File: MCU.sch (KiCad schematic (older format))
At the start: 32 parts, among them IC1 STM32G474RET6, SW1 RST, SW2 SW_DIP_x04, U14 MCP2562-E-SN, U15 ST1480ABDR, U16 AM26LV32ACPWR, U17 SI8621AB-B-ISR, Y1 Resonator_Small

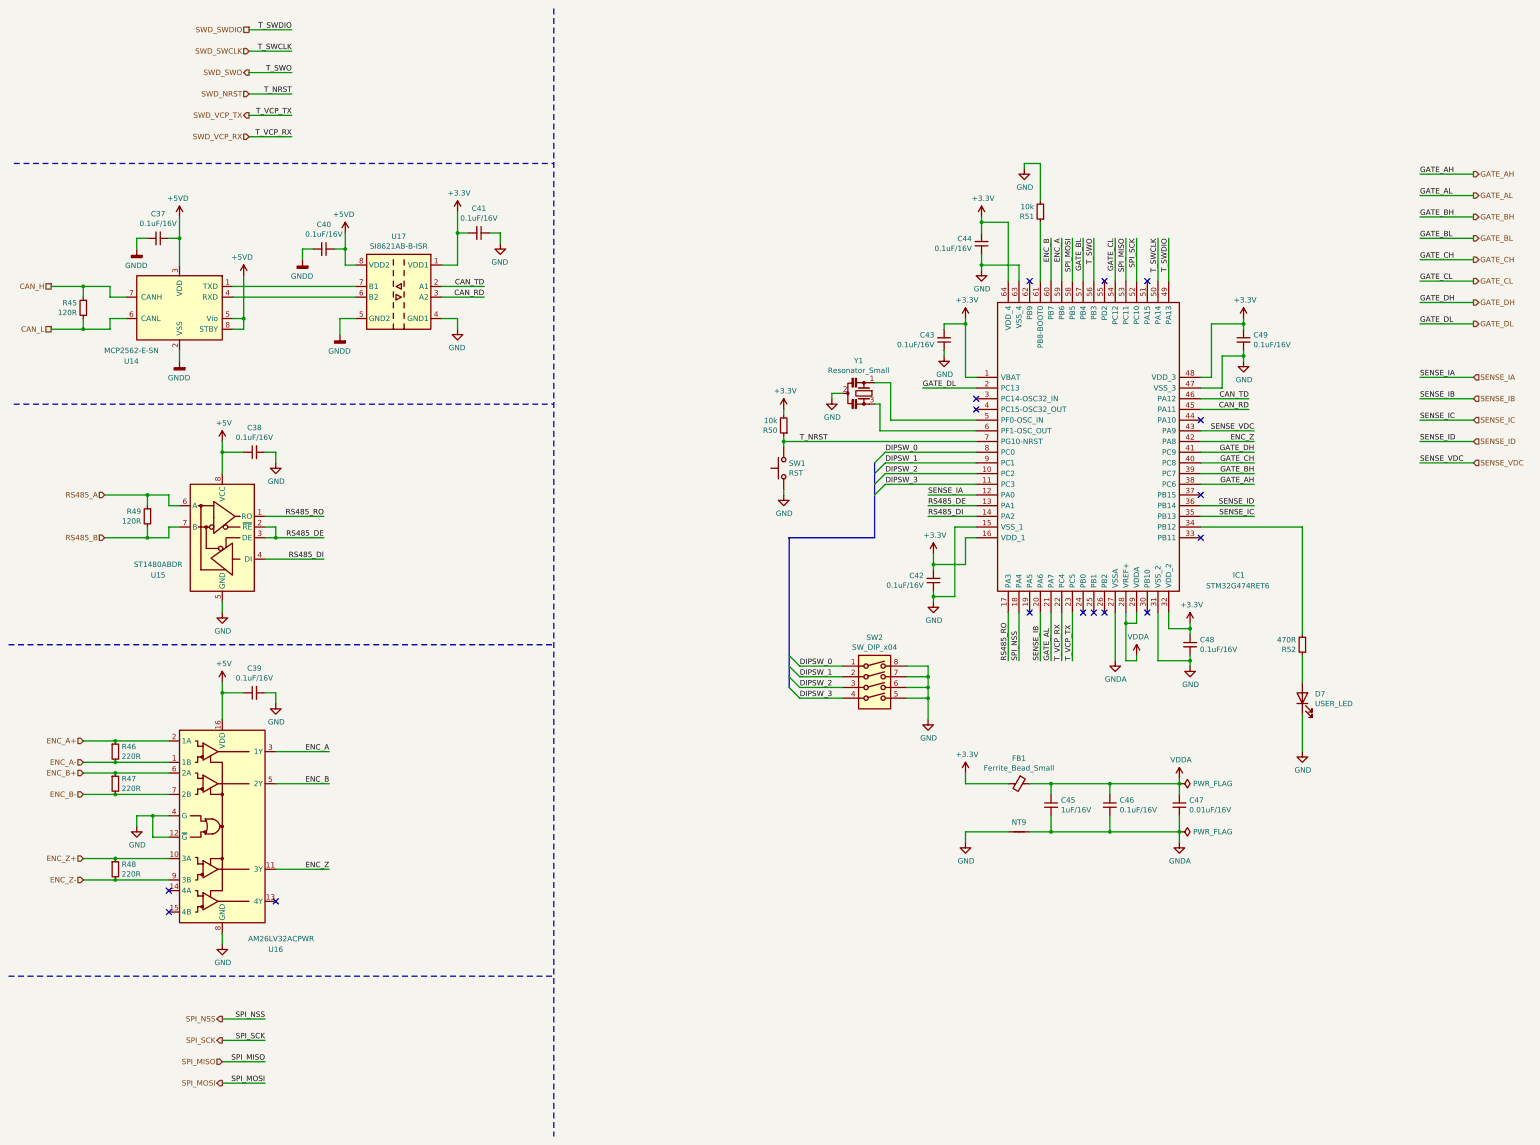
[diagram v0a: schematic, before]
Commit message: Update: 回路図、DCリンクCap1つ削除、アノテーションリセット
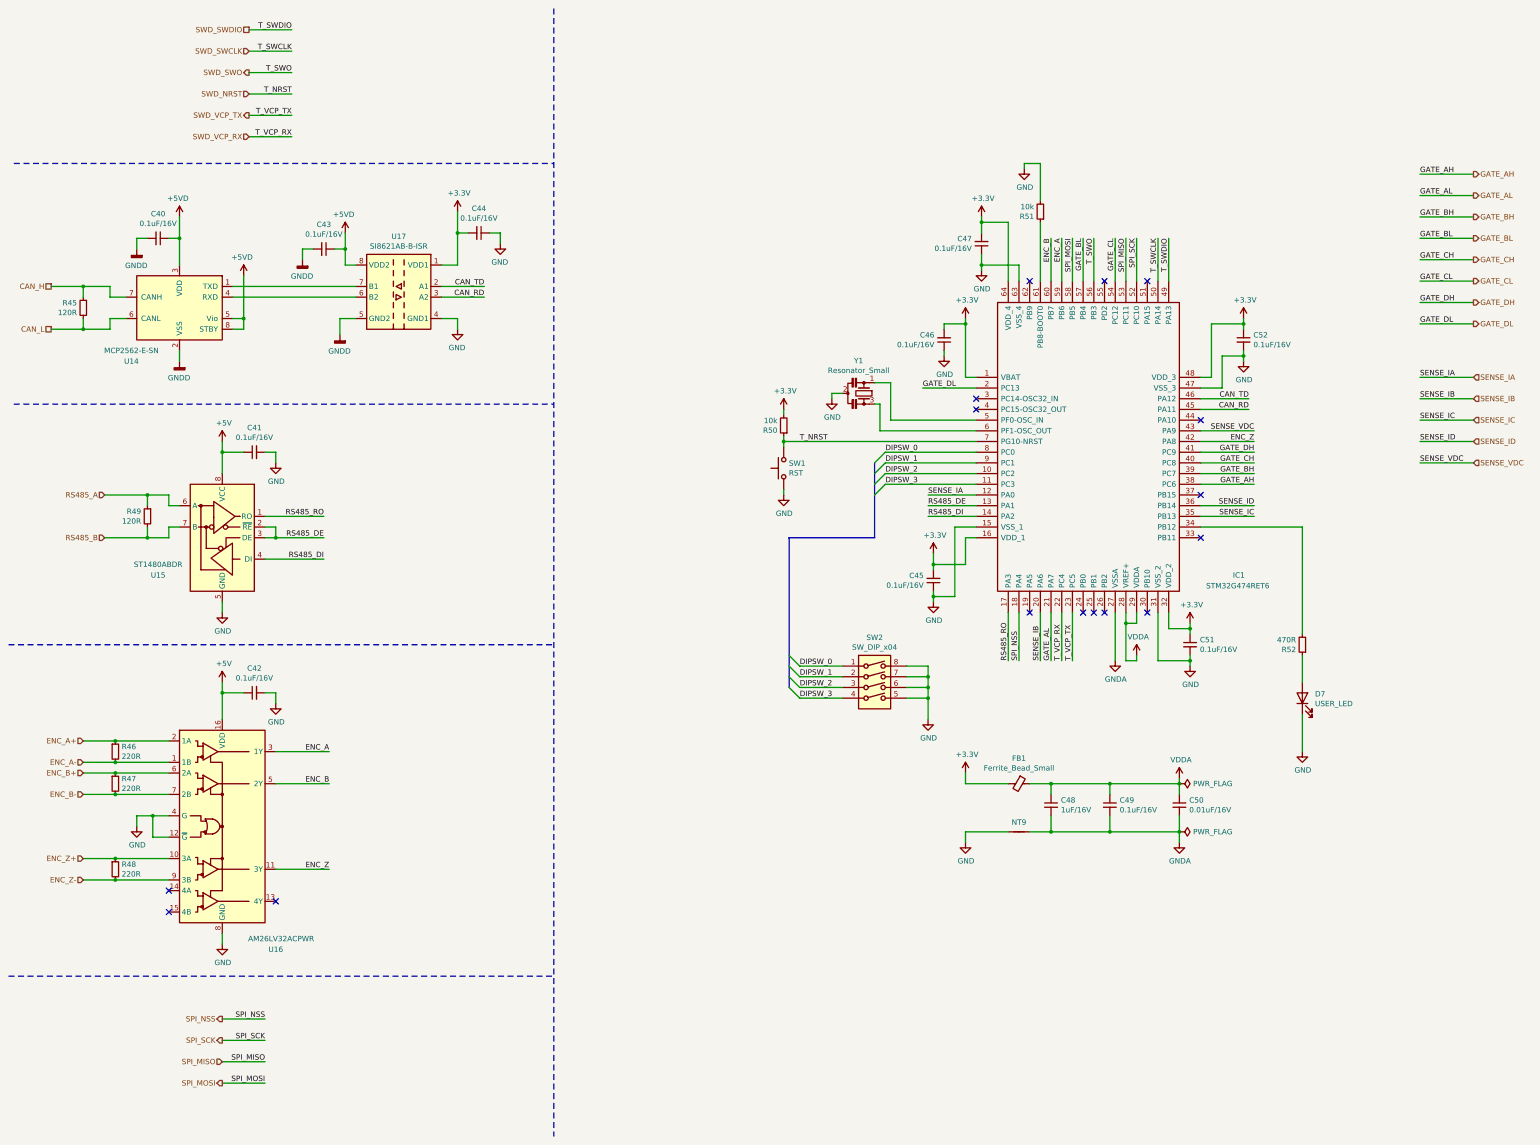
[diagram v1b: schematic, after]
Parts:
- renumbered C37 to C40, C38 to C41, C39 to C42, C40 to C43, C41 to C44, C42 to C45, C43 to C46, C44 to C47, C45 to C48, C46 to C49, C47 to C50, C48 to C51, C49 to C52
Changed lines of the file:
@@
 P 9750 3000
 AR Path="/6081BB0D" Ref="#PWR?"  Part="1"
-AR Path="/607D8C01/6081BB0D" Ref="#PWR0100"  Part="1"
-F 0 "#PWR0100" H 9750 2750 50  0001 C CNN
+AR Path="/607D8C01/6081BB0D" Ref="#PWR0102"  Part="1"
+F 0 "#PWR0102" H 9750 2750 50  0001 C CNN
 F 1 "GND" H 9755 2827 50  0000 C CNN
 F 2 "" H 9750 3000 50  0001 C CNN
@@
 P 9600 8350
 AR Path="/6081BB3C" Ref="#PWR?"  Part="1"
-AR Path="/607D8C01/6081BB3C" Ref="#PWR0102"  Part="1"
-F 0 "#PWR0102" H 9600 8100 50  0001 C CNN
+AR Path="/607D8C01/6081BB3C" Ref="#PWR0100"  Part="1"
+F 0 "#PWR0100" H 9600 8100 50  0001 C CNN
 F 1 "GND" H 9605 8177 50  0000 C CNN
 F 2 "" H 9600 8350 50  0001 C CNN
@@
 P 10400 8000
 AR Path="/6081BB44" Ref="C?"  Part="1"
-AR Path="/607D8C01/6081BB44" Ref="C45"  Part="1"
-F 0 "C45" H 10492 8046 50  0000 L CNN
+AR Path="/607D8C01/6081BB44" Ref="C48"  Part="1"
+F 0 "C48" H 10492 8046 50  0000 L CNN
 F 1 "1uF/16V" H 10492 7955 50  0000 L CNN
 F 2 "Capacitor_SMD:C_0603_1608Metric" H 10400 8000 50  0001 C CNN
@@
 P 10950 8000
 AR Path="/6081BB4A" Ref="C?"  Part="1"
-AR Path="/607D8C01/6081BB4A" Ref="C46"  Part="1"
-F 0 "C46" H 11042 8046 50  0000 L CNN
+AR Path="/607D8C01/6081BB4A" Ref="C49"  Part="1"
+F 0 "C49" H 11042 8046 50  0000 L CNN
 F 1 "0.1uF/16V" H 11042 7955 50  0000 L CNN
 F 2 "Capacitor_SMD:C_0603_1608Metric" H 10950 8000 50  0001 C CNN
@@
 P 11600 8000
 AR Path="/6081BB50" Ref="C?"  Part="1"
-AR Path="/607D8C01/6081BB50" Ref="C47"  Part="1"
-F 0 "C47" H 11692 8046 50  0000 L CNN
+AR Path="/607D8C01/6081BB50" Ref="C50"  Part="1"
+F 0 "C50" H 11692 8046 50  0000 L CNN
 F 1 "0.01uF/16V" H 11692 7955 50  0000 L CNN
 F 2 "Capacitor_SMD:C_0603_1608Metric" H 11600 8000 50  0001 C CNN
@@
 P 9400 3650
 AR Path="/6081BB7F" Ref="C?"  Part="1"
-AR Path="/607D8C01/6081BB7F" Ref="C43"  Part="1"
-F 0 "C43" H 9309 3604 50  0000 R CNN
+AR Path="/607D8C01/6081BB7F" Ref="C46"  Part="1"
+F 0 "C46" H 9309 3604 50  0000 R CNN
 F 1 "0.1uF/16V" H 9309 3695 50  0000 R CNN
 F 2 "Capacitor_SMD:C_0603_1608Metric" H 9400 3650 50  0001 C CNN
@@
 P 9300 5900
 AR Path="/6081BB8A" Ref="C?"  Part="1"
-AR Path="/607D8C01/6081BB8A" Ref="C42"  Part="1"
-F 0 "C42" H 9209 5854 50  0000 R CNN
+AR Path="/607D8C01/6081BB8A" Ref="C45"  Part="1"
+F 0 "C45" H 9209 5854 50  0000 R CNN
 F 1 "0.1uF/16V" H 9209 5945 50  0000 R CNN
 F 2 "Capacitor_SMD:C_0603_1608Metric" H 9300 5900 50  0001 C CNN
@@
 P 11700 6500
 AR Path="/6081BB95" Ref="C?"  Part="1"
-AR Path="/607D8C01/6081BB95" Ref="C48"  Part="1"
-F 0 "C48" H 11792 6546 50  0000 L CNN
+AR Path="/607D8C01/6081BB95" Ref="C51"  Part="1"
+F 0 "C51" H 11792 6546 50  0000 L CNN
 F 1 "0.1uF/16V" H 11792 6455 50  0000 L CNN
 F 2 "Capacitor_SMD:C_0603_1608Metric" H 11700 6500 50  0001 C CNN
@@
 P 12200 3650
 AR Path="/6081BBB0" Ref="C?"  Part="1"
-AR Path="/607D8C01/6081BBB0" Ref="C49"  Part="1"
-F 0 "C49" H 12292 3696 50  0000 L CNN
+AR Path="/607D8C01/6081BBB0" Ref="C52"  Part="1"
+F 0 "C52" H 12292 3696 50  0000 L CNN
 F 1 "0.1uF/16V" H 12292 3605 50  0000 L CNN
 F 2 "Capacitor_SMD:C_0603_1608Metric" H 12200 3650 50  0001 C CNN
@@
 P 9750 2750
 AR Path="/6081BC36" Ref="C?"  Part="1"
-AR Path="/607D8C01/6081BC36" Ref="C44"  Part="1"
-F 0 "C44" H 9659 2704 50  0000 R CNN
+AR Path="/607D8C01/6081BC36" Ref="C47"  Part="1"
+F 0 "C47" H 9659 2704 50  0000 R CNN
 F 1 "0.1uF/16V" H 9659 2795 50  0000 R CNN
 F 2 "Capacitor_SMD:C_0603_1608Metric" H 9750 2750 50  0001 C CNN
@@
 	4850 2950 4700 2950
 $Comp
-L Device:C_Small C37
+L Device:C_Small C40
 U 1 1 5D63A863
 P 2050 2700
-F 0 "C37" V 2279 2700 50  0000 C CNN
+F 0 "C40" V 2279 2700 50  0000 C CNN
 F 1 "0.1uF/16V" V 2188 2700 50  0000 C CNN
 F 2 "Capacitor_SMD:C_0603_1608Metric" H 2050 2700 50  0001 C CNN
@@
 	3800 2950 3900 2950
 $Comp
-L Device:C_Small C40
+L Device:C_Small C43
 U 1 1 5D654E8E
 P 3600 2800
-F 0 "C40" V 3829 2800 50  0000 C CNN
+F 0 "C43" V 3829 2800 50  0000 C CNN
 F 1 "0.1uF/16V" V 3738 2800 50  0000 C CNN
 F 2 "Capacitor_SMD:C_0603_1608Metric" H 3600 2800 50  0001 C CNN
@@
 	3400 2800 3400 2900
 $Comp
-L Device:C_Small C41
+L Device:C_Small C44
 U 1 1 5D66021A
 P 5050 2650
-F 0 "C41" V 5279 2650 50  0000 C CNN
+F 0 "C44" V 5279 2650 50  0000 C CNN
 F 1 "0.1uF/16V" V 5188 2650 50  0000 C CNN
 F 2 "Capacitor_SMD:C_0603_1608Metric" H 5050 2650 50  0001 C CNN
@@
 RS485_DI
 $Comp
-L Device:C_Small C38
+L Device:C_Small C41
 U 1 1 6207F667
 P 2950 4700
-F 0 "C38" V 3179 4700 50  0000 C CNN
+F 0 "C41" V 3179 4700 50  0000 C CNN
 F 1 "0.1uF/16V" V 3088 4700 50  0000 C CNN
 F 2 "Capacitor_SMD:C_0603_1608Metric" H 2950 4700 50  0001 C CNN
@@
 	2650 6850 2650 6950
 $Comp
-L Device:C_Small C39
+L Device:C_Small C42
 U 1 1 62180D5B
 P 2950 6950
-F 0 "C39" V 3179 6950 50  0000 C CNN
+F 0 "C42" V 3179 6950 50  0000 C CNN
 F 1 "0.1uF/16V" V 3088 6950 50  0000 C CNN
 F 2 "Capacitor_SMD:C_0603_1608Metric" H 2950 6950 50  0001 C CNN
@@
 P 9600 7700
 AR Path="/63184AE5" Ref="#PWR?"  Part="1"
-AR Path="/607D8C01/63184AE5" Ref="#PWR0101"  Part="1"
-F 0 "#PWR0101" H 9600 7550 50  0001 C CNN
+AR Path="/607D8C01/63184AE5" Ref="#PWR099"  Part="1"
+F 0 "#PWR099" H 9600 7550 50  0001 C CNN
 F 1 "+3.3V" H 9615 7873 50  0000 C CNN
 F 2 "" H 9600 7700 50  0001 C CNN
@@
 P 9750 2500
 AR Path="/6321E3A4" Ref="#PWR?"  Part="1"
-AR Path="/607D8C01/6321E3A4" Ref="#PWR099"  Part="1"
-F 0 "#PWR099" H 9750 2350 50  0001 C CNN
+AR Path="/607D8C01/6321E3A4" Ref="#PWR0101"  Part="1"
+F 0 "#PWR0101" H 9750 2350 50  0001 C CNN
 F 1 "+3.3V" H 9765 2673 50  0000 C CNN
 F 2 "" H 9750 2500 50  0001 C CNN
@@
 NoConn ~ 10200 3100
 $Comp
-L power:PWR_FLAG #FLG0109
+L power:PWR_FLAG #FLG08
 U 1 1 63940CAC
 P 11600 8250
-F 0 "#FLG0109" H 11600 8325 50  0001 C CNN
+F 0 "#FLG08" H 11600 8325 50  0001 C CNN
 F 1 "PWR_FLAG" V 11600 8378 50  0000 L CNN
 F 2 "" H 11600 8250 50  0001 C CNN
@@
 $EndComp
 $Comp
-L power:PWR_FLAG #FLG0110
+L power:PWR_FLAG #FLG07
 U 1 1 63941F34
 P 11600 7800
-F 0 "#FLG0110" H 11600 7875 50  0001 C CNN
+F 0 "#FLG07" H 11600 7875 50  0001 C CNN
 F 1 "PWR_FLAG" V 11600 7928 50  0000 L CNN
 F 2 "" H 11600 7800 50  0001 C CNN

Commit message: Update: アナログリファレンスをLDOからに変更
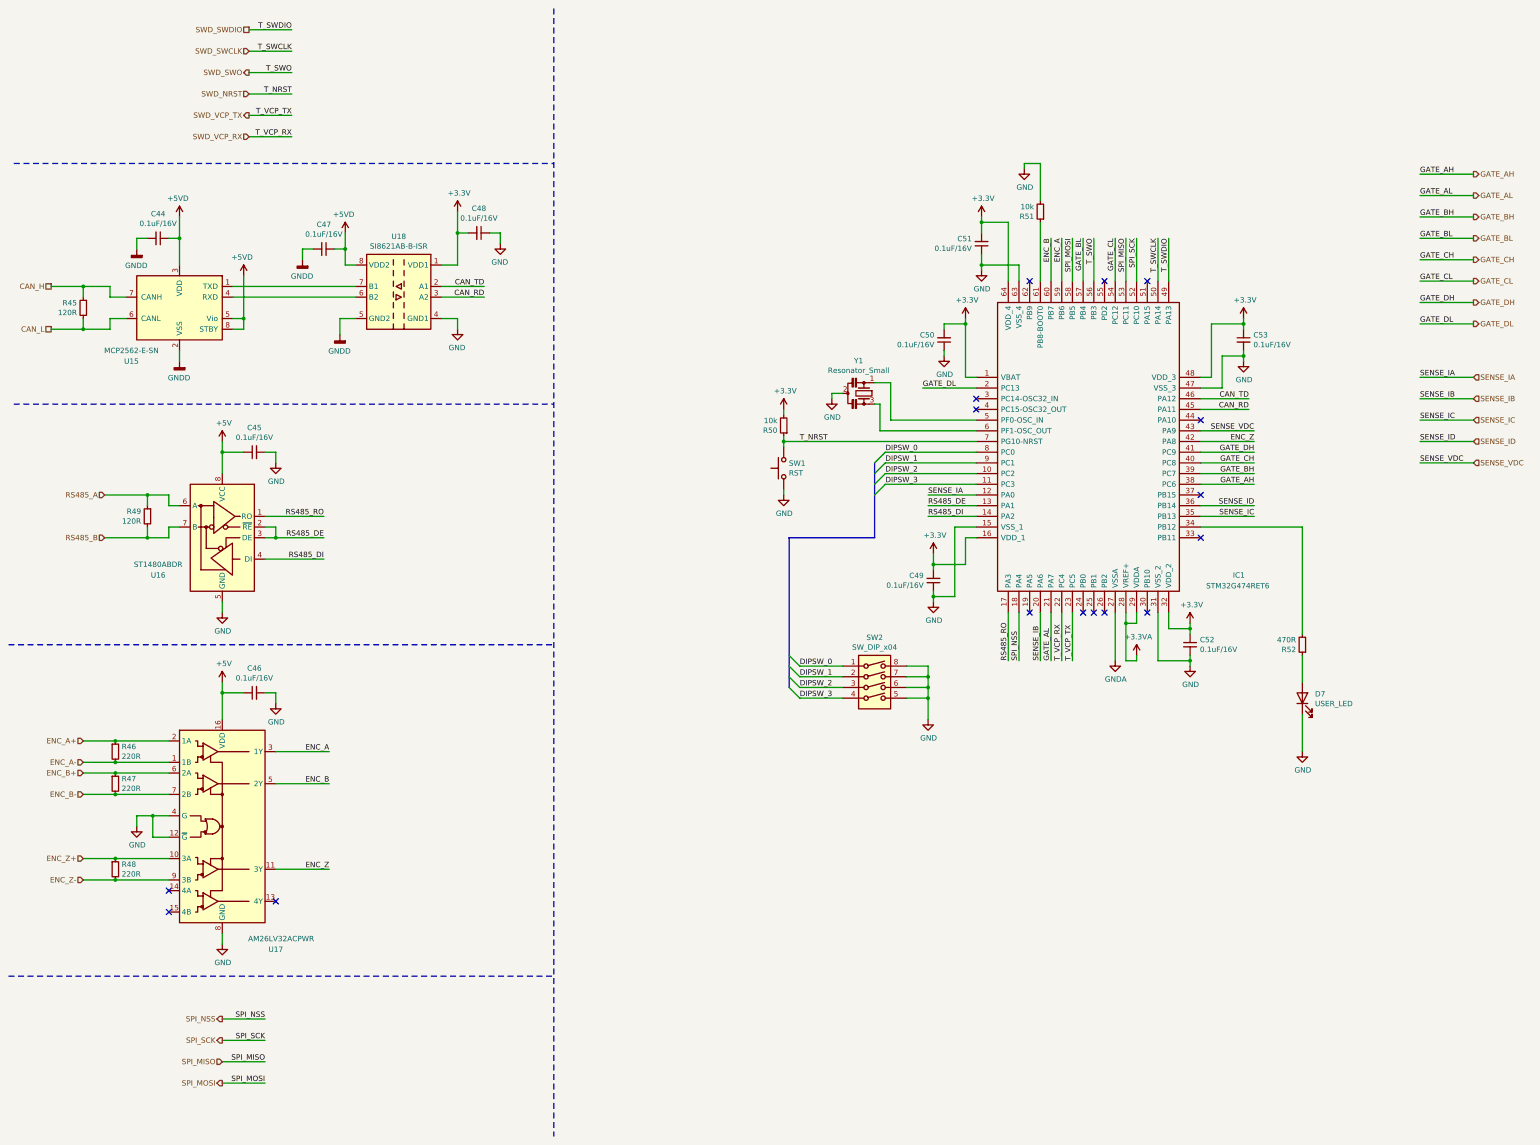
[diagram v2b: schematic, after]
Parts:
- removed C48: 1uF/16V, Capacitor_SMD:C_0603_1608Metric, symbol Device:C_Small
- removed C49: 0.1uF/16V, Capacitor_SMD:C_0603_1608Metric, symbol Device:C_Small
- removed C50: 0.01uF/16V, Capacitor_SMD:C_0603_1608Metric, symbol Device:C_Small
- removed FB1: Ferrite_Bead_Small, Inductor_SMD:L_0603_1608Metric, symbol Device:Ferrite_Bead_Small
- removed NT9: Net-Tie_2, NetTie:NetTie-2_SMD_Pad0.5mm, symbol Device:Net-Tie_2
- renumbered C40 to C44, C41 to C45, C42 to C46, C43 to C47, C44 to C48, C45 to C49, C46 to C50, C47 to C51, C51 to C52, C52 to C53, U14 to U15, U15 to U16, U16 to U17, U17 to U18
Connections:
- net VDDA renamed +3.3VA

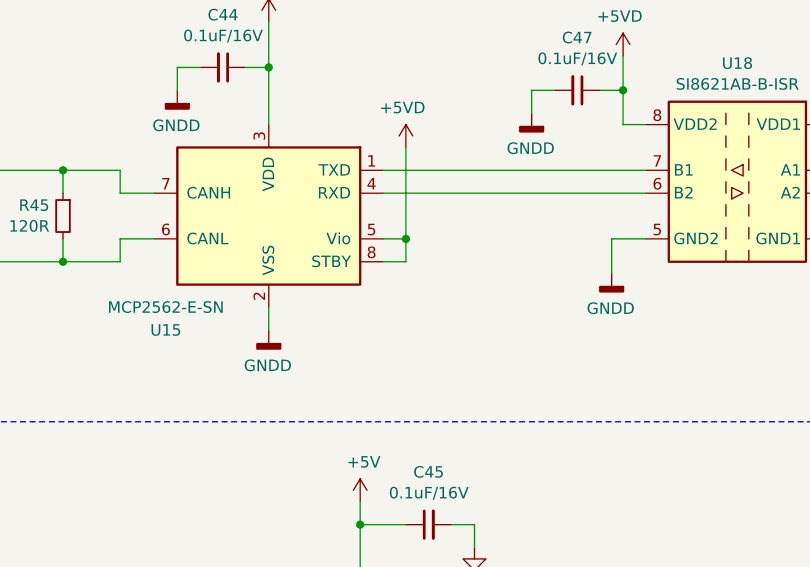
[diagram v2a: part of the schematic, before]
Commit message: wip CAN STBYピン修正
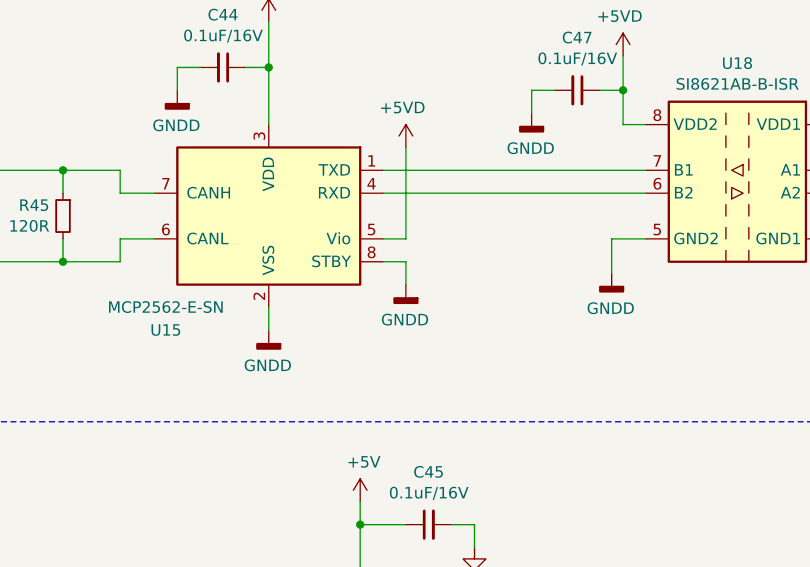
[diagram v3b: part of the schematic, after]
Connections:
- net +5VD: no longer U15.8 (STBY)
- net GNDD: now also U15.8 (STBY)
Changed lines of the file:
@@
 	2750 3550 2850 3550
 Wire Wire Line
-	2850 3550 2850 3450
-Connection ~ 2850 3450
+	2850 3650 2850 3550
 Wire Wire Line
 	3900 3150 2750 3150
@@
 	1    0    0    -1
 $EndComp
+$Comp
+L power:GNDD #PWR?
+U 1 1 60CCC792
+P 2850 3650
+AR Path="/60CCC792" Ref="#PWR?"  Part="1"
+AR Path="/607D8C01/60CCC792" Ref="#PWR?"  Part="1"
+F 0 "#PWR?" H 2850 3400 50  0001 C CNN
+F 1 "GNDD" H 2854 3495 50  0000 C CNN
+F 2 "" H 2850 3650 50  0001 C CNN
+F 3 "" H 2850 3650 50  0001 C CNN
+	1    2850 3650
+	-1   0    0    -1
+$EndComp
 Wire Bus Line
